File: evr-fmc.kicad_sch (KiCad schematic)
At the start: 0 parts

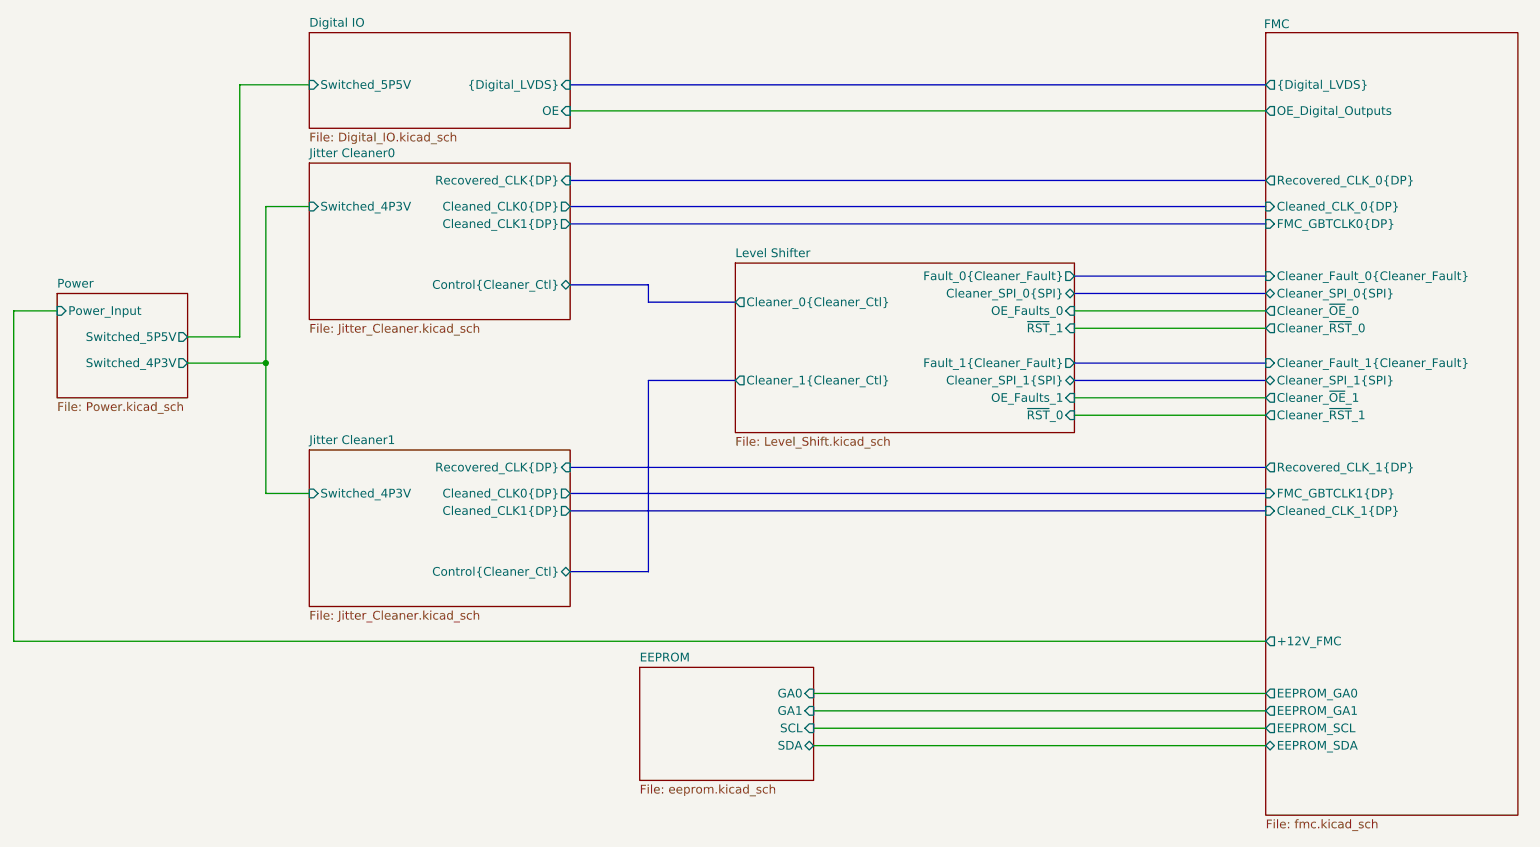
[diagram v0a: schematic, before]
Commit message: Routed LVDS lines
- Routed LVDS lines
- Swapped some digital output pairs
- Properly connected the output enable signal for digital outputs in the schematic
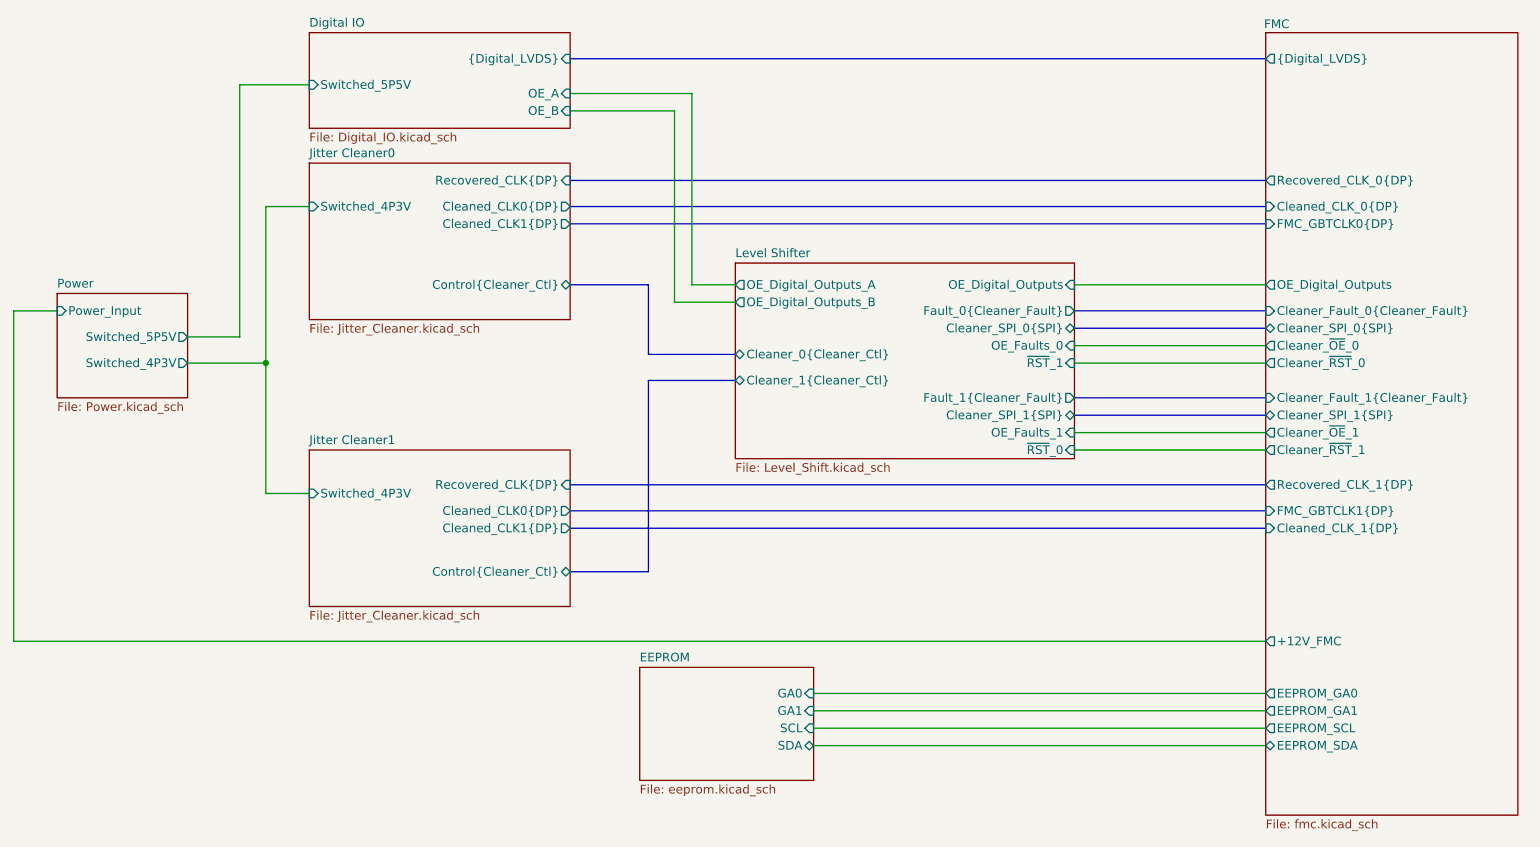
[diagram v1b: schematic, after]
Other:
- sheet Digital IO ports: added OE_A, OE_B; removed OE
- sheet Level Shifter ports: added OE_Digital_Outputs, OE_Digital_Outputs_A, OE_Digital_Outputs_B; removed none

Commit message: Finished Draft Layout
- Finished Draft Layout
- Changed Switcher IC
- Added extra decoupling caps for digital output spikes
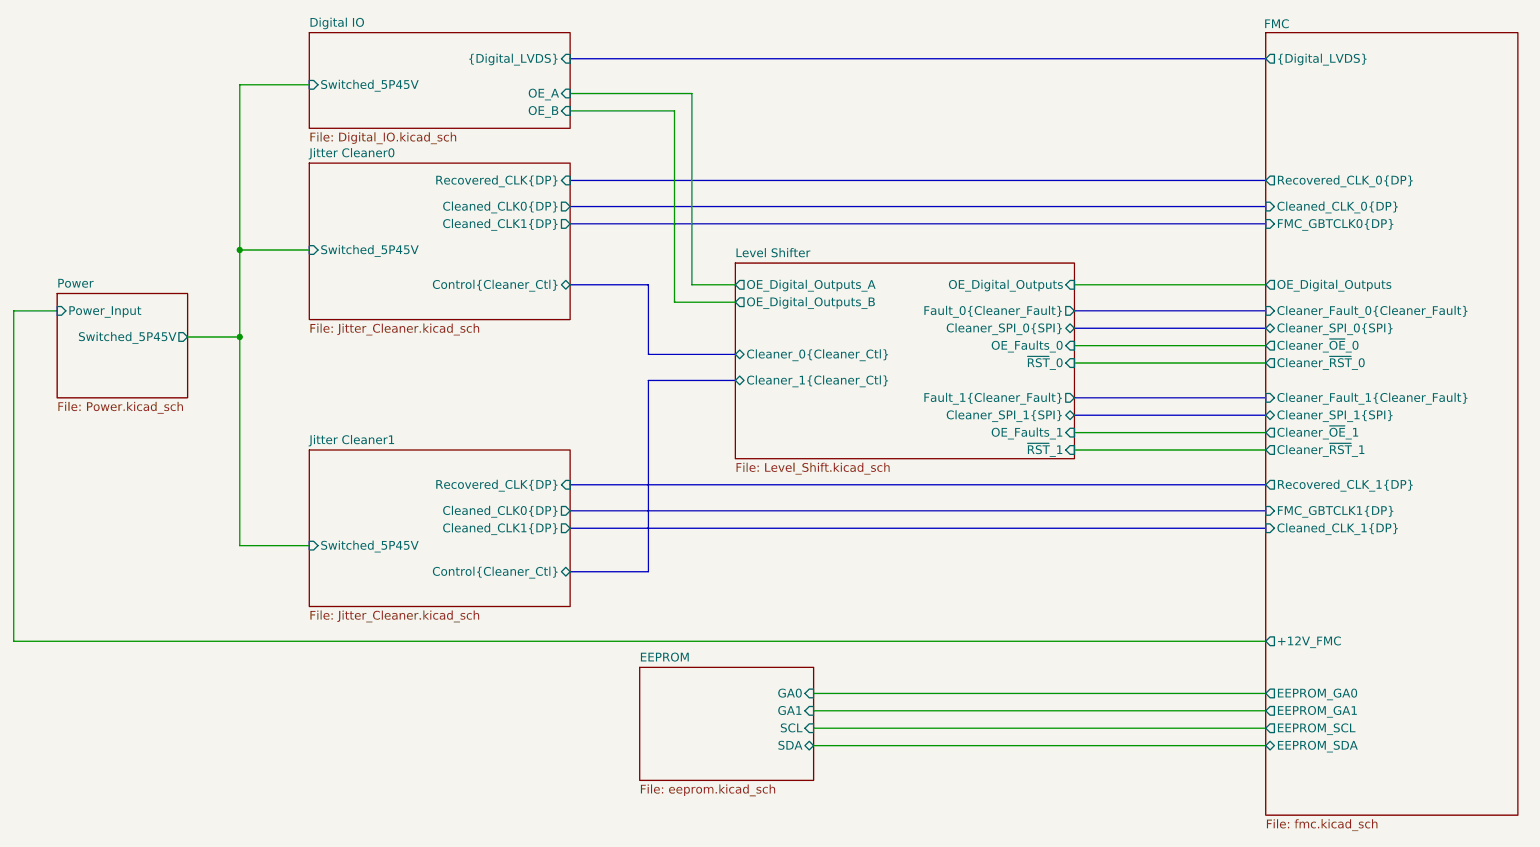
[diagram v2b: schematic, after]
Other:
- sheet Digital IO ports: added Switched_5P45V; removed Switched_5P5V
- sheet Jitter Cleaner0 ports: added Switched_5P45V; removed Switched_4P3V
- sheet Jitter Cleaner1 ports: added Switched_5P45V; removed Switched_4P3V
- sheet Power ports: added Switched_5P45V; removed Switched_4P3V, Switched_5P5V
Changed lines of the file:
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@@
 	)
 	(junction
-		(at 62.23 88.9)
+		(at 58.42 72.39)
 		(diameter 0)
 		(color 0 0 0 0)
 	)
+	(junction
+		(at 58.42 85.09)
+		(diameter 0)
+		(color 0 0 0 0)
+	)
 	(wire
 		(pts
@@
 	(wire
 		(pts
-			(xy 58.42 85.09) (xy 58.42 48.26)
-		)
-		(stroke
-			(width 0)
-			(type default)
-		)
-	)
-	(wire
-		(pts
-			(xy 62.23 66.04) (xy 62.23 88.9)
+			(xy 58.42 48.26) (xy 58.42 72.39)
 		)
 		(stroke
@@
 	(wire
 		(pts
+			(xy 68.58 115.57) (xy 58.42 115.57)
+		)
+		(stroke
+			(width 0)
+			(type default)
+		)
+	)
+	(wire
+		(pts
 			(xy 180.34 77.47) (xy 208.28 77.47)
 		)
@@
 	(wire
 		(pts
-			(xy 68.58 66.04) (xy 62.23 66.04)
-		)
-		(stroke
-			(width 0)
-			(type default)
-		)
-	)
-	(wire
-		(pts
 			(xy 25.4 81.28) (xy 31.75 81.28)
 		)
@@
 		)
 	)
+	(wire
+		(pts
+			(xy 58.42 72.39) (xy 58.42 85.09)
+		)
+		(stroke
+			(width 0)
+			(type default)
+		)
+	)
 	(bus
 		(pts
@@
 	(wire
 		(pts
+			(xy 58.42 115.57) (xy 58.42 85.09)
+		)
+		(stroke
+			(width 0)
+			(type default)
+		)
+	)
+	(wire
+		(pts
 			(xy 180.34 101.6) (xy 208.28 101.6)
 		)
@@
 		)
 	)
-	(wire
-		(pts
-			(xy 62.23 107.95) (xy 68.58 107.95)
-		)
-		(stroke
-			(width 0)
-			(type default)
-		)
-	)
 	(bus
 		(pts
@@
 		)
 	)
-	(wire
-		(pts
-			(xy 50.8 88.9) (xy 62.23 88.9)
-		)
-		(stroke
-			(width 0)
-			(type default)
-		)
-	)
 	(bus
 		(pts
@@
 	(wire
 		(pts
-			(xy 62.23 88.9) (xy 62.23 107.95)
-		)
-		(stroke
-			(width 0)
-			(type default)
-		)
-	)
-	(wire
-		(pts
 			(xy 180.34 99.06) (xy 208.28 99.06)
 		)
@@
 		(pts
 			(xy 142.24 137.16) (xy 208.28 137.16)
+		)
+		(stroke
+			(width 0)
+			(type default)
+		)
+	)
+	(wire
+		(pts
+			(xy 68.58 72.39) (xy 58.42 72.39)
 		)
 		(stroke
@@
 		)
 		(pin "~{RST}_0" input
+			(at 180.34 88.9 0)
+			(effects
+				(font
+					(size 1.27 1.27)
+				)
+				(justify right)
+			)
+		)
+		(pin "~{RST}_1" input
 			(at 180.34 101.6 0)
-			(effects
-				(font
-					(size 1.27 1.27)
-				)
-				(justify right)
-			)
-		)
-		(pin "~{RST}_1" input
-			(at 180.34 88.9 0)
 			(effects
 				(font
@@
 			)
 		)
-		(pin "Switched_4P3V" input
-			(at 68.58 107.95 180)
-			(effects
-				(font
-					(size 1.27 1.27)
-				)
-				(justify left)
-			)
-		)
 		(pin "Control{Cleaner_Ctl}" bidirectional
 			(at 106.68 119.38 0)
@@
 				)
 				(justify right)
+			)
+		)
+		(pin "Switched_5P45V" input
+			(at 68.58 115.57 180)
+			(effects
+				(font
+					(size 1.27 1.27)
+				)
+				(justify left)
 			)
 		)
@@
 			)
 		)
-		(pin "Switched_4P3V" input
-			(at 68.58 66.04 180)
+		(pin "Switched_5P45V" input
+			(at 68.58 72.39 180)
 			(effects
 				(font
@@
 			)
 		)
-		(pin "Switched_4P3V" output
-			(at 50.8 88.9 0)
-			(effects
-				(font
-					(size 1.27 1.27)
-				)
-				(justify right)
-			)
-		)
-		(pin "Switched_5P5V" output
+		(pin "Switched_5P45V" output
 			(at 50.8 85.09 0)
 			(effects
@@
 			)
 		)
-		(pin "Switched_5P5V" input
-			(at 68.58 48.26 180)
-			(effects
-				(font
-					(size 1.27 1.27)
-				)
-				(justify left)
-			)
-		)
 		(pin "{Digital_LVDS}" input
 			(at 106.68 44.45 0)
@@
 			)
 		)
+		(pin "Switched_5P45V" input
+			(at 68.58 48.26 180)
+			(effects
+				(font
+					(size 1.27 1.27)
+				)
+				(justify left)
+			)
+		)
